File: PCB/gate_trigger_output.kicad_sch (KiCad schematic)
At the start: 9 parts, among them J2 OUTa, J3 OUTb, Q2 BC547

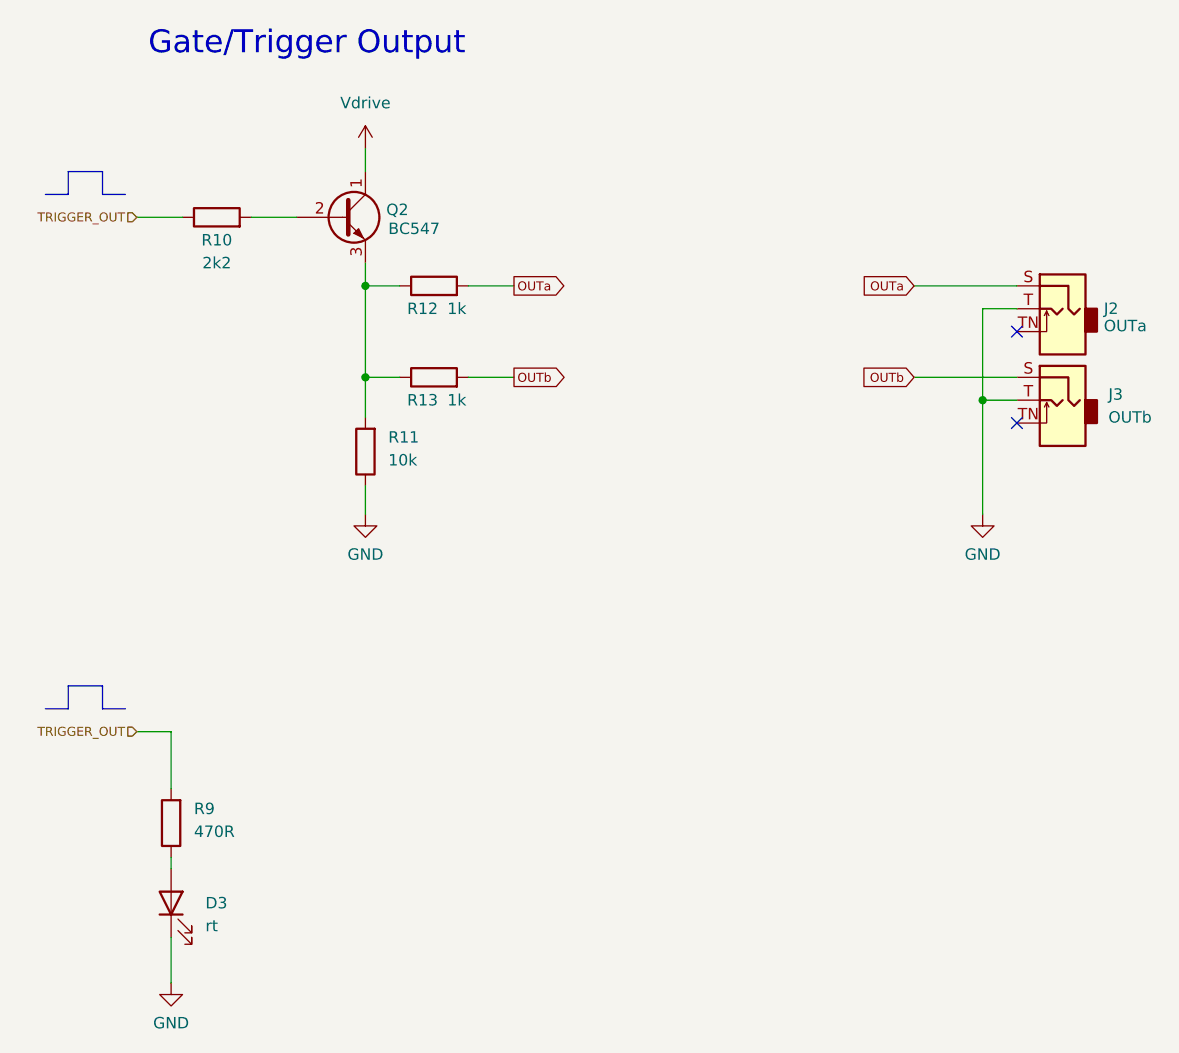
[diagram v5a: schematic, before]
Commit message: :sparkles: Add PCB layout for the module
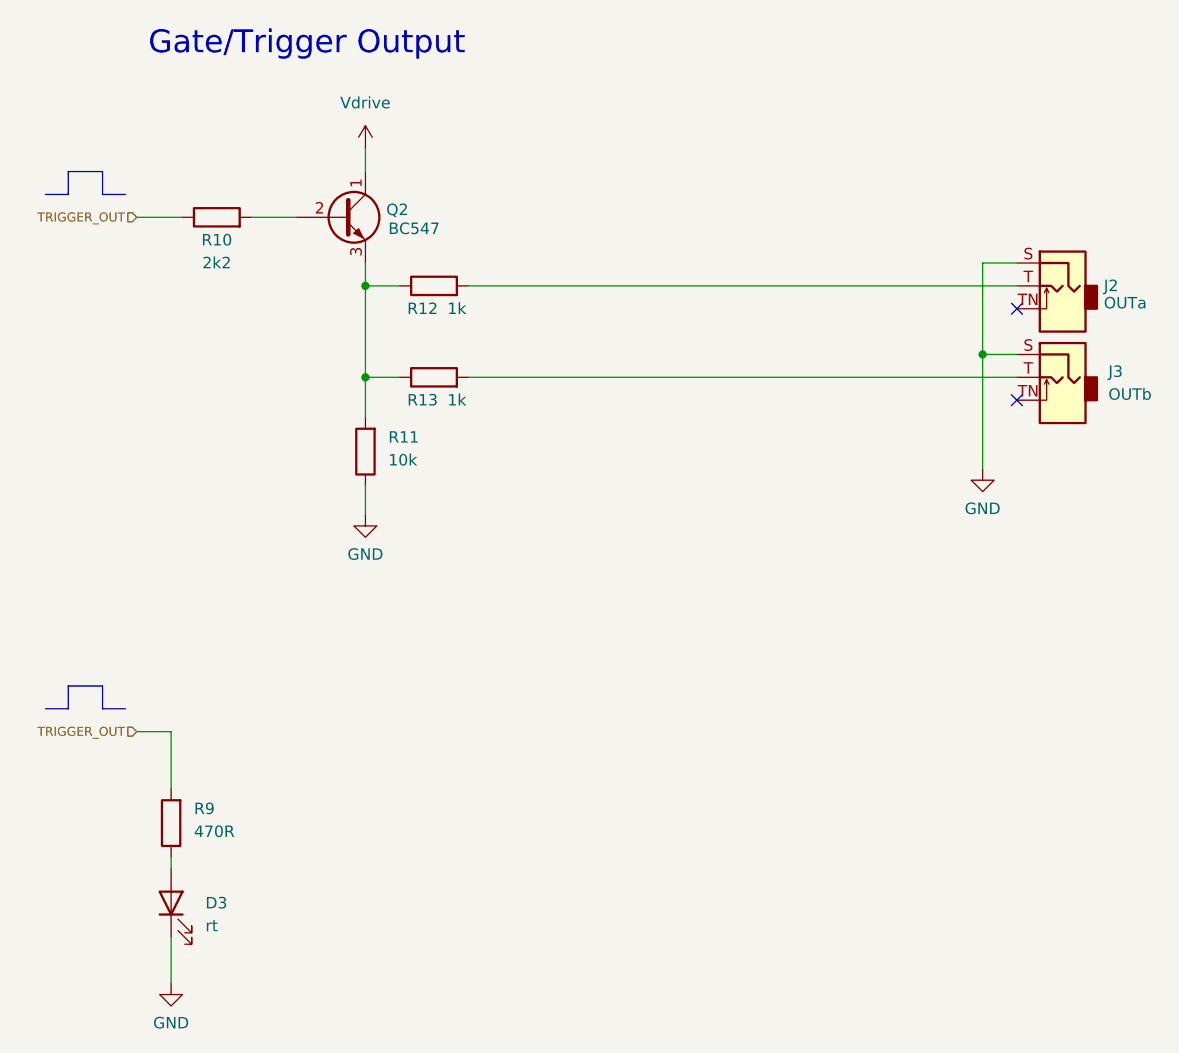
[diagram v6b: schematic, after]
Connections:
- net GND: now also J2.S, J3.S; no longer J2.T, J3.T
- net OUTa: no longer names the net of R12.2
- net OUTa: now also J2.T; no longer J2.S
- net OUTb: no longer names the net of R13.2
- net OUTb: now also J3.T; no longer J3.S
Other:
- moved on the sheet: J2, J3
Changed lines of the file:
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@@
     (company "moPsy")
   )
-  (junction (at 127 64.77) (diameter 0) (color 0 0 0 0)
+  (junction (at 127 59.69) (diameter 0) (color 0 0 0 0)
   )
   (junction (at 58.42 52.07) (diameter 0) (color 0 0 0 0)
@@
   (junction (at 58.42 62.23) (diameter 0) (color 0 0 0 0)
   )
-  (no_connect (at 130.81 67.31))
-  (no_connect (at 130.81 57.15))
-  (wire (pts (xy 119.38 62.23) (xy 130.81 62.23))
-    (stroke (width 0) (type default))
-  )
-  (wire (pts (xy 69.85 52.07) (xy 74.93 52.07))
-    (stroke (width 0) (type default))
-  )
+  (no_connect (at 130.81 64.77))
+  (no_connect (at 130.81 54.61))
   (polyline (pts (xy 25.4 39.37) (xy 25.4 41.91))
     (stroke (width 0) (type solid))
@@
     (stroke (width 0) (type solid))
   )
-  (wire (pts (xy 130.81 54.61) (xy 127 54.61))
+  (wire (pts (xy 130.81 49.53) (xy 127 49.53))
     (stroke (width 0) (type default))
   )
@@
     (stroke (width 0) (type solid))
   )
-  (wire (pts (xy 119.38 52.07) (xy 130.81 52.07))
-    (stroke (width 0) (type default))
-  )
   (polyline (pts (xy 25.4 41.91) (xy 22.86 41.91))
     (stroke (width 0) (type solid))
   )
+  (wire (pts (xy 69.85 62.23) (xy 130.81 62.23))
+    (stroke (width 0) (type default))
+  )
   (wire (pts (xy 58.42 74.295) (xy 58.42 77.47))
     (stroke (width 0) (type default))
@@
     (stroke (width 0) (type default))
   )
+  (wire (pts (xy 69.85 52.07) (xy 130.81 52.07))
+    (stroke (width 0) (type default))
+  )
   (wire (pts (xy 36.83 115.57) (xy 36.83 116.84))
     (stroke (width 0) (type default))
   )
-  (wire (pts (xy 127 64.77) (xy 130.81 64.77))
+  (wire (pts (xy 127 59.69) (xy 130.81 59.69))
     (stroke (width 0) (type default))
   )
@@
     (stroke (width 0) (type default))
   )
-  (wire (pts (xy 127 54.61) (xy 127 64.77))
+  (wire (pts (xy 127 49.53) (xy 127 59.69))
     (stroke (width 0) (type default))
   )
@@
     (stroke (width 0) (type default))
   )
-  (wire (pts (xy 127 64.77) (xy 127 77.47))
+  (wire (pts (xy 127 59.69) (xy 127 72.39))
     (stroke (width 0) (type default))
   )
@@
   )
   (wire (pts (xy 33.02 44.45) (xy 38.1 44.45))
-    (stroke (width 0) (type default))
-  )
-  (wire (pts (xy 69.85 62.23) (xy 74.93 62.23))
     (stroke (width 0) (type default))
   )
@@
     (effects (font (size 2.54 2.54)) (justify left bottom))
   )
-  (global_label "OUTa" (shape output) (at 74.93 52.07 0) (fields_autoplaced)
-    (effects (font (size 1 1)) (justify left))
-    (property "Intersheetrefs" "${INTERSHEET_REFS}" (at 80.5919 52.0075 0)
-      (effects (font (size 1 1)) (justify left) hide)
-    )
-  )
-  (global_label "OUTb" (shape input) (at 119.38 62.23 180) (fields_autoplaced)
-    (effects (font (size 1 1)) (justify right))
-    (property "Intersheetrefs" "${INTERSHEET_REFS}" (at 113.7181 62.1675 0)
-      (effects (font (size 1 1)) (justify right) hide)
-    )
-  )
-  (global_label "OUTb" (shape output) (at 74.93 62.23 0) (fields_autoplaced)
-    (effects (font (size 1 1)) (justify left))
-    (property "Intersheetrefs" "${INTERSHEET_REFS}" (at 80.5919 62.1675 0)
-      (effects (font (size 1 1)) (justify left) hide)
-    )
-  )
-  (global_label "OUTa" (shape input) (at 119.38 52.07 180) (fields_autoplaced)
-    (effects (font (size 1 1)) (justify right))
-    (property "Intersheetrefs" "${INTERSHEET_REFS}" (at 113.7181 52.0075 0)
-      (effects (font (size 1 1)) (justify right) hide)
-    )
-  )
   (hierarchical_label "TRIGGER_OUT" (shape input) (at 33.02 101.6 180) (fields_autoplaced)
     (effects (font (size 1 1)) (justify right))
@@
     (effects (font (size 1 1)) (justify right))
   )
-  (symbol (lib_id "Connector:AudioJack2_Ground_SwitchT") (at 135.89 54.61 0) (mirror y) (unit 1)
+  (symbol (lib_id "Connector:AudioJack2_Ground_SwitchT") (at 135.89 52.07 0) (mirror y) (unit 1)
     (in_bom yes) (on_board yes) (dnp no) (fields_autoplaced)
-    (property "Reference" "J2" (at 140.462 54.6013 0)
-      (effects (font (size 1.27 1.27)) (justify right))
-    )
-    (property "Value" "OUTa" (at 140.462 56.5223 0)
-      (effects (font (size 1.27 1.27)) (justify right))
-    )
-    (property "Footprint" "moPsy:Jack_3.5mm_QingPu_WQP-PJ398SM_Vertical_CircularHoles_Centered" (at 135.89 54.61 0)
-      (effects (font (size 1.27 1.27)) hide)
-    )
-    (property "Datasheet" "~" (at 135.89 54.61 0)
+    (property "Reference" "J2" (at 140.462 52.0613 0)
+      (effects (font (size 1.27 1.27)) (justify right))
+    )
+    (property "Value" "OUTa" (at 140.462 53.9823 0)
+      (effects (font (size 1.27 1.27)) (justify right))
+    )
+    (property "Footprint" "moPsy:Jack_3.5mm_QingPu_WQP-PJ398SM_Vertical_CircularHoles_Centered" (at 135.89 52.07 0)
+      (effects (font (size 1.27 1.27)) hide)
+    )
+    (property "Datasheet" "~" (at 135.89 52.07 0)
       (effects (font (size 1.27 1.27)) hide)
     )
@@
     )
   )
-  (symbol (lib_id "power:GND") (at 127 77.47 0) (unit 1)
+  (symbol (lib_id "power:GND") (at 127 72.39 0) (unit 1)
     (in_bom yes) (on_board yes) (dnp no) (fields_autoplaced)
-    (property "Reference" "#PWR014" (at 127 83.82 0)
-      (effects (font (size 1.27 1.27)) hide)
-    )
-    (property "Value" "GND" (at 127 81.9134 0)
-      (effects (font (size 1.27 1.27)))
-    )
-    (property "Footprint" "" (at 127 77.47 0)
-      (effects (font (size 1.27 1.27)) hide)
-    )
-    (property "Datasheet" "" (at 127 77.47 0)
+    (property "Reference" "#PWR014" (at 127 78.74 0)
+      (effects (font (size 1.27 1.27)) hide)
+    )
+    (property "Value" "GND" (at 127 76.8334 0)
+      (effects (font (size 1.27 1.27)))
+    )
+    (property "Footprint" "" (at 127 72.39 0)
+      (effects (font (size 1.27 1.27)) hide)
+    )
+    (property "Datasheet" "" (at 127 72.39 0)
       (effects (font (size 1.27 1.27)) hide)
     )
@@
     )
   )
-  (symbol (lib_id "Connector:AudioJack2_Ground_SwitchT") (at 135.89 64.77 0) (mirror y) (unit 1)
+  (symbol (lib_id "Connector:AudioJack2_Ground_SwitchT") (at 135.89 62.23 0) (mirror y) (unit 1)
     (in_bom yes) (on_board yes) (dnp no) (fields_autoplaced)
-    (property "Reference" "J3" (at 140.97 64.1349 0)
-      (effects (font (size 1.27 1.27)) (justify right))
-    )
-    (property "Value" "OUTb" (at 140.97 66.6749 0)
-      (effects (font (size 1.27 1.27)) (justify right))
-    )
-    (property "Footprint" "moPsy:Jack_3.5mm_QingPu_WQP-PJ398SM_Vertical_CircularHoles_Centered" (at 135.89 64.77 0)
-      (effects (font (size 1.27 1.27)) hide)
-    )
-    (property "Datasheet" "~" (at 135.89 64.77 0)
-      (effects (font (size 1.27 1.27)) hide)
-    )
+    (property "Reference" "J3" (at 140.97 61.5949 0)
+      (effects (font (size 1.27 1.27)) (justify right))
+    )
+    (property "Value" "OUTb" (at 140.97 64.1349 0)
+      (effects (font (size 1.27 1.27)) (justify right))
+    )
+    (property "Footprint" "moPsy:Jack_3.5mm_QingPu_WQP-PJ398SM_Vertical_CircularHoles_Centered" (at 135.89 62.23 0)
+      (effects (font (size 1.27 1.27)) hide)
+    )
+    (property "Datasheet" "~" (at 135.89 62.23 0)
+      (effects (font (size 1.27 1.27)) hide)
+    )

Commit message: :hammer: Change transistor footprints to hand-solder variant
This fixes #56
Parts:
- Q2: footprint Package_TO_SOT_THT:TO-92_Inline -> Package_TO_SOT_THT:TO-92_HandSolder
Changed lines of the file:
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@@
       (effects (font (size 1.27 1.27)) (justify left))
     )
-    (property "Footprint" "Package_TO_SOT_THT:TO-92_Inline" (at 60.96 46.355 0)
+    (property "Footprint" "Package_TO_SOT_THT:TO-92_HandSolder" (at 60.96 46.355 0)
       (effects (font (size 1.27 1.27) italic) (justify left) hide)
     )
